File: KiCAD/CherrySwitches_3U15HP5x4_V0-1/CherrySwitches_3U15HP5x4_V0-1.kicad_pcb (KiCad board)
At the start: 2 copper layers, 76.2 x 128.5 mm, 28 parts, among them J1 Conn_02x05_Odd_Even, J2 Conn_02x05_Odd_Even, J3 Conn_02x05_Odd_Even, J4 Conn_02x05_Odd_Even, SW1 SW_SPST, SW10 SW_SPST, SW11 SW_SPST, SW12 SW_SPST, SW13 SW_SPST, SW14 SW_SPST, SW15 SW_SPST, SW16 SW_SPST, SW17 SW_SPST, SW18 SW_SPST, SW19 SW_SPST, SW2 SW_SPST, SW20 SW_SPST, SW3 SW_SPST, SW4 SW_SPST, SW5 SW_SPST, SW6 SW_SPST, SW7 SW_SPST, SW8 SW_SPST, SW9 SW_SPST

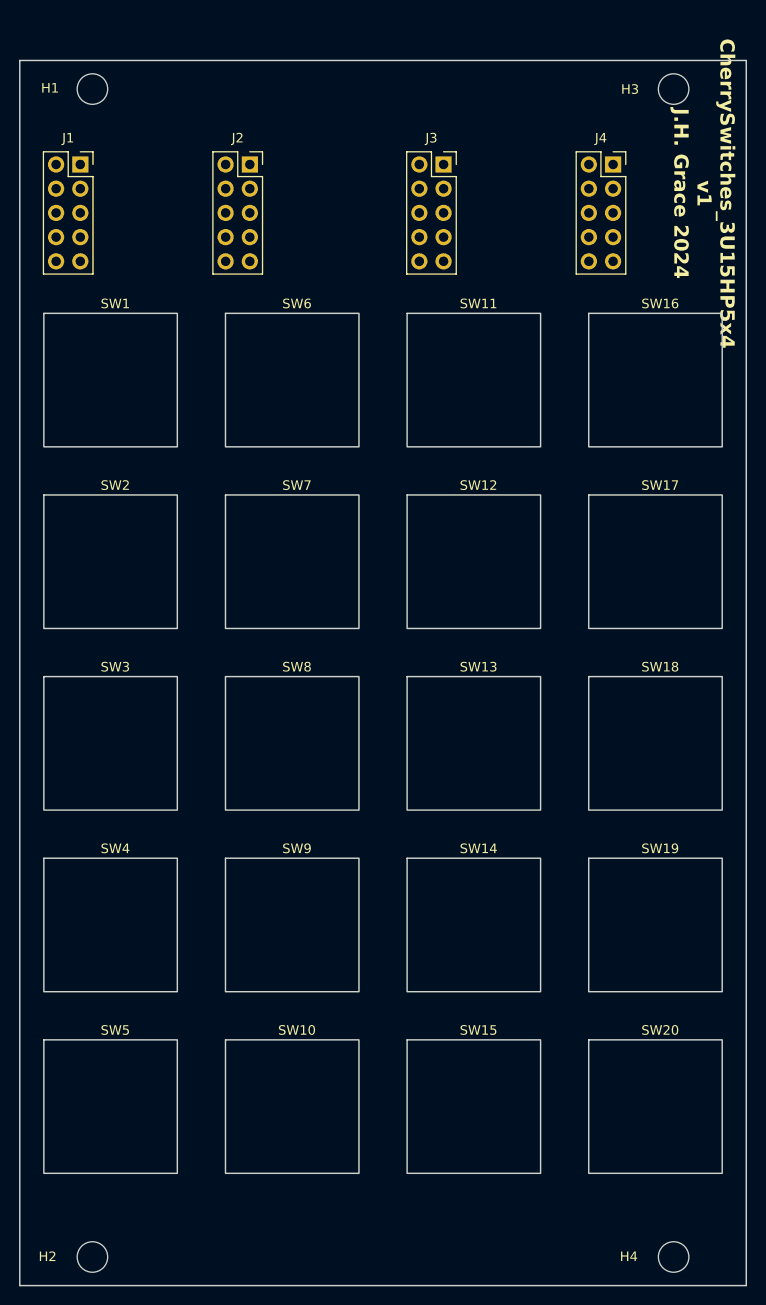
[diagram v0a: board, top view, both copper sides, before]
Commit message: updated PCB widths to better conform to Eurorack standards
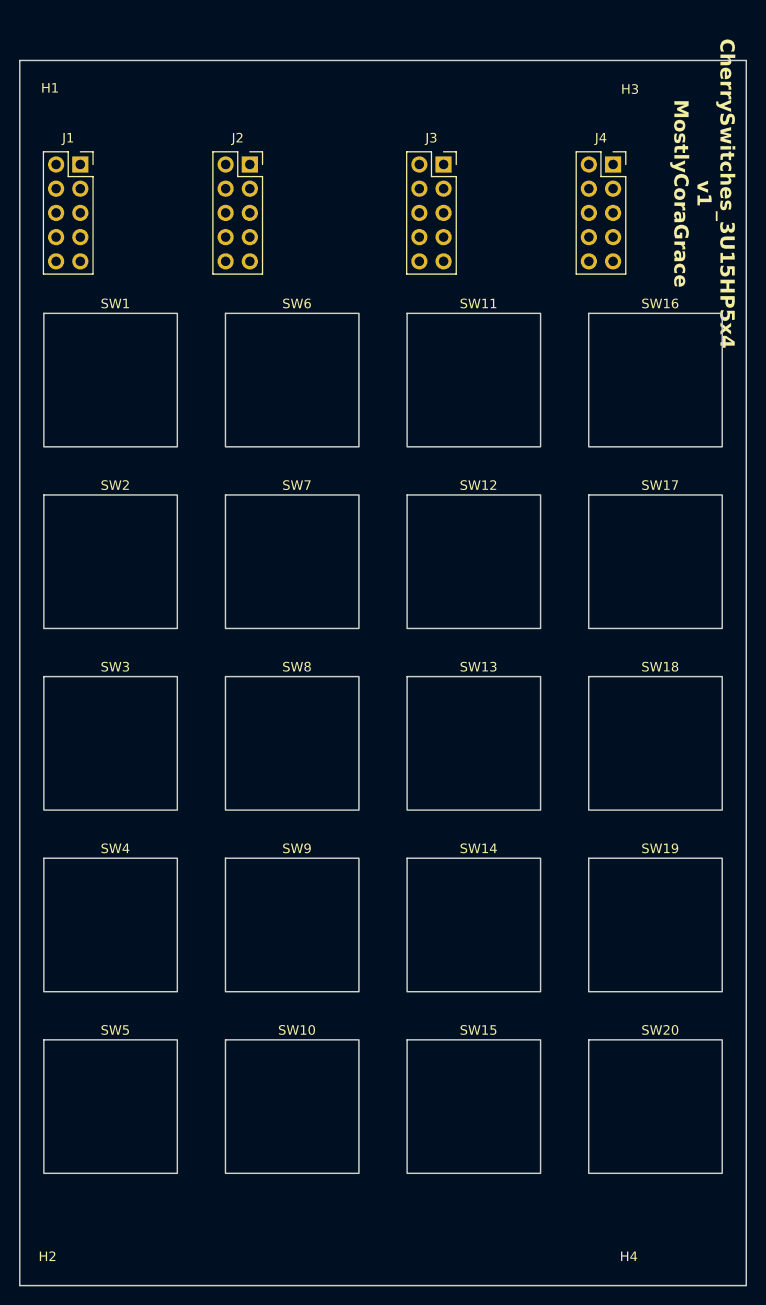
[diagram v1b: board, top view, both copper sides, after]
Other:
- board text added: "CherrySwitches_3U15HP5x4 v1 MostlyCoraGrace"
- board text removed: "CherrySwitches_3U15HP5x4 v1 J.H. Grace 2024"
